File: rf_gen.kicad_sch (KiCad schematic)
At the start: 41 parts, among them J1 Conn_01x07_Male, J2 Conn_01x02_Female, J3 Conn_01x04_Male, J4 Jack-DC, Q1 GS61004B, Q2 G3R350MT12J, U1 NPC81074, U2 AP62150

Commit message: Added Mouser BOM
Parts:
- L8: footprint (none) -> Inductor_SMD:L_0805_2012Metric
- R3, R4: footprint (none) -> Resistor_SMD:R_0805_2012Metric
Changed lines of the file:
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@@
     (property "Reference" "L8" (id 0) (at 200.66 115.57 90))
     (property "Value" "3.3u" (id 1) (at 200.66 118.11 90))
-    (property "Footprint" "" (id 2) (at 200.66 121.92 0)
+    (property "Footprint" "Inductor_SMD:L_0805_2012Metric" (id 2) (at 200.66 121.92 0)
       (effects (font (size 1.27 1.27)) hide)
     )
@@
       (effects (font (size 1.27 1.27)) (justify left))
     )
-    (property "Footprint" "" (id 2) (at 194.056 125.984 90)
+    (property "Footprint" "Resistor_SMD:R_0805_2012Metric" (id 2) (at 194.056 125.984 90)
       (effects (font (size 1.27 1.27)) hide)
     )
@@
       (effects (font (size 1.27 1.27)) (justify left))
     )
-    (property "Footprint" "" (id 2) (at 194.056 136.144 90)
+    (property "Footprint" "Resistor_SMD:R_0805_2012Metric" (id 2) (at 194.056 136.144 90)
       (effects (font (size 1.27 1.27)) hide)
     )
@@
     )
     (path "/12596e45-6707-4319-9f3d-fd07bfb54475"
-      (reference "L8") (unit 1) (value "3.3u") (footprint "")
+      (reference "L8") (unit 1) (value "3.3u") (footprint "Inductor_SMD:L_0805_2012Metric")
     )
     (path "/98c6b453-1edb-41b3-980c-820933811e74"
@@
     )
     (path "/7acdfc10-c7b8-4964-a5bd-7fbb6a01d10b"
-      (reference "R3") (unit 1) (value "52.3k") (footprint "")
+      (reference "R3") (unit 1) (value "52.3k") (footprint "Resistor_SMD:R_0805_2012Metric")
     )
     (path "/7db06bf3-c515-4f51-9e87-096535d2035f"
-      (reference "R4") (unit 1) (value "10k") (footprint "")
+      (reference "R4") (unit 1) (value "10k") (footprint "Resistor_SMD:R_0805_2012Metric")
     )
     (path "/05524bb0-81b6-47ef-ac3c-1b815742ae84"

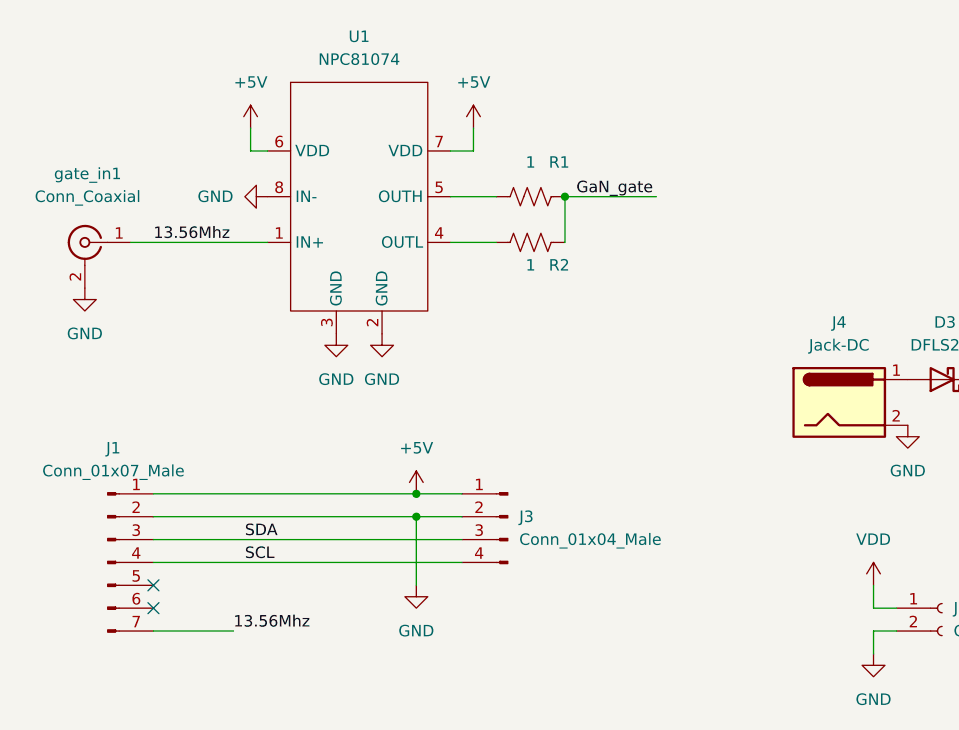
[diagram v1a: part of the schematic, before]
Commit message: Added CoilCraft footprints
Using approximate footprints for the toroids for now
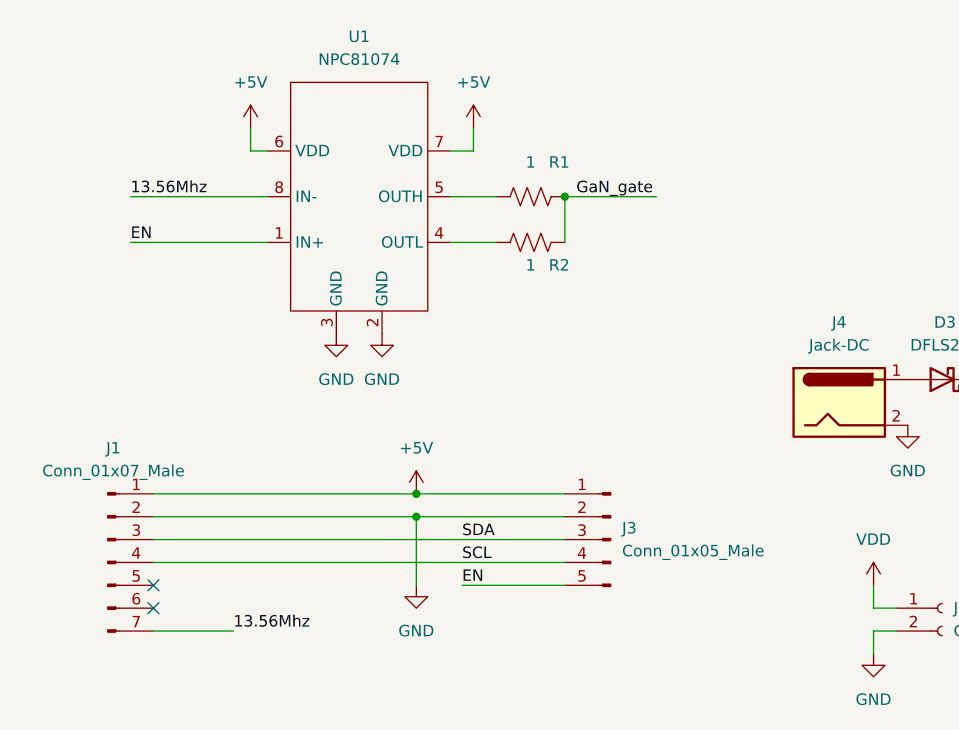
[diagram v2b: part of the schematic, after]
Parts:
- removed J3: Conn_01x04_Male, symbol Connector:Conn_01x04_Male
- removed gate_in1: Conn_Coaxial, Connector_Coaxial:SMA_Amphenol_901-144_Vertical, symbol Connector:Conn_Coaxial
- added J3: Conn_01x05_Male, Connector_PinHeader_2.54mm:PinHeader_1x05_P2.54mm_Vertical, symbol Connector:Conn_01x05_Male
- C13, C15, C16: footprint (none) -> Capacitor_SMD:C_1206_3216Metric
- C14: footprint (none) -> Capacitor_SMD:C_0805_2012Metric
- J1: footprint (none) -> Connector_PinHeader_2.54mm:PinHeader_1x07_P2.54mm_Vertical
- J2: footprint (none) -> Connector_Phoenix_MC_HighVoltage:PhoenixContact_MCV_1,5_2-GF-5.08_1x02_P5.08mm_Vertical_ThreadedFlange
- J4: footprint (none) -> Connector_BarrelJack:BarrelJack_SwitchcraftConxall_RAPC10U_Horizontal
- L1: footprint (none) -> rf_gen:2222SQ-221
- L2, L6: footprint (none) -> Inductor_THT:L_Toroid_Vertical_L10.0mm_W5.0mm_P5.08mm
- L3: footprint (none) -> rf_gen:2222SQ-90N
- L4: footprint (none) -> rf_gen:2222SQ-111
- L5: footprint (none) -> Inductor_THT:L_Axial_L17.5mm_D12.0mm_P20.32mm_Horizontal_Vishay_IM-10-46
- L7: footprint (none) -> Inductor_THT:L_Toroid_Vertical_L28.6mm_W14.3mm_P11.43mm_Bourns_5700
- rf_out1: footprint (none) -> Connector_Coaxial:BNC_TEConnectivity_1478204_Vertical
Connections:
- net +5V: now also J3.1 (Pin_1)
- net 13.56Mhz: now also U1.8 (IN-); no longer U1.1 (IN+)
- net GND: now also J3.2 (Pin_2); no longer U1.8 (IN-)
- net SCL: now also J3.4 (Pin_4)
- net SDA: now also J3.3 (Pin_3)
- new net EN: J3.5 (Pin_5), U1.1 (IN+)

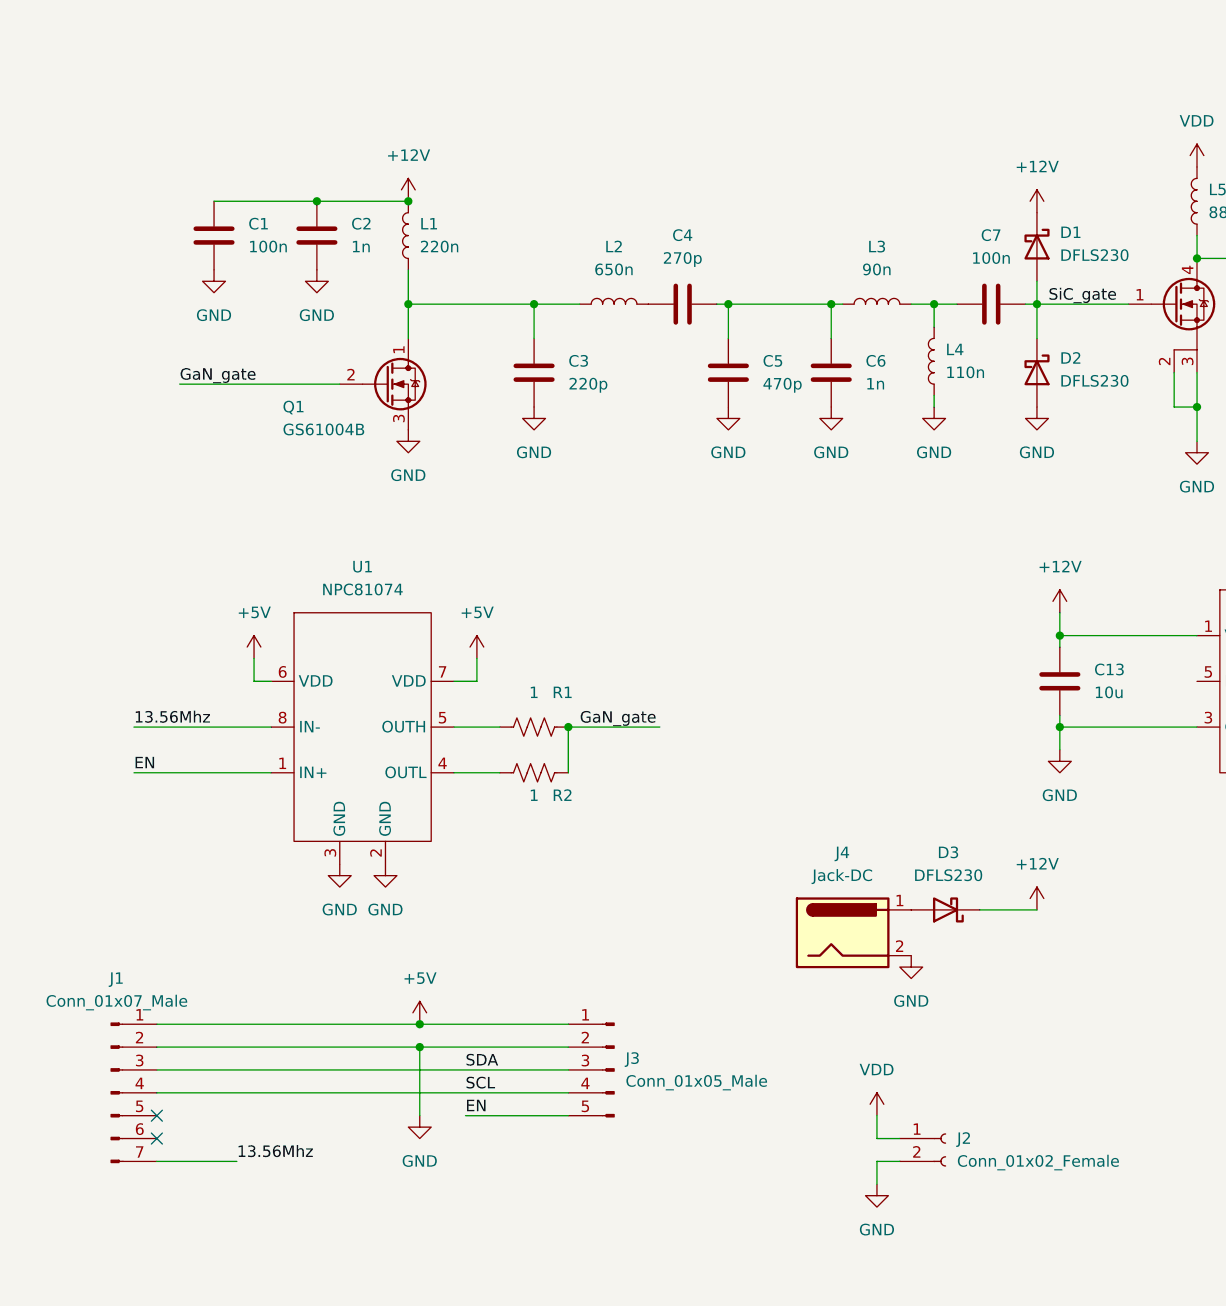
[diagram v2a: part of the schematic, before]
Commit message: First draft of PCB layout
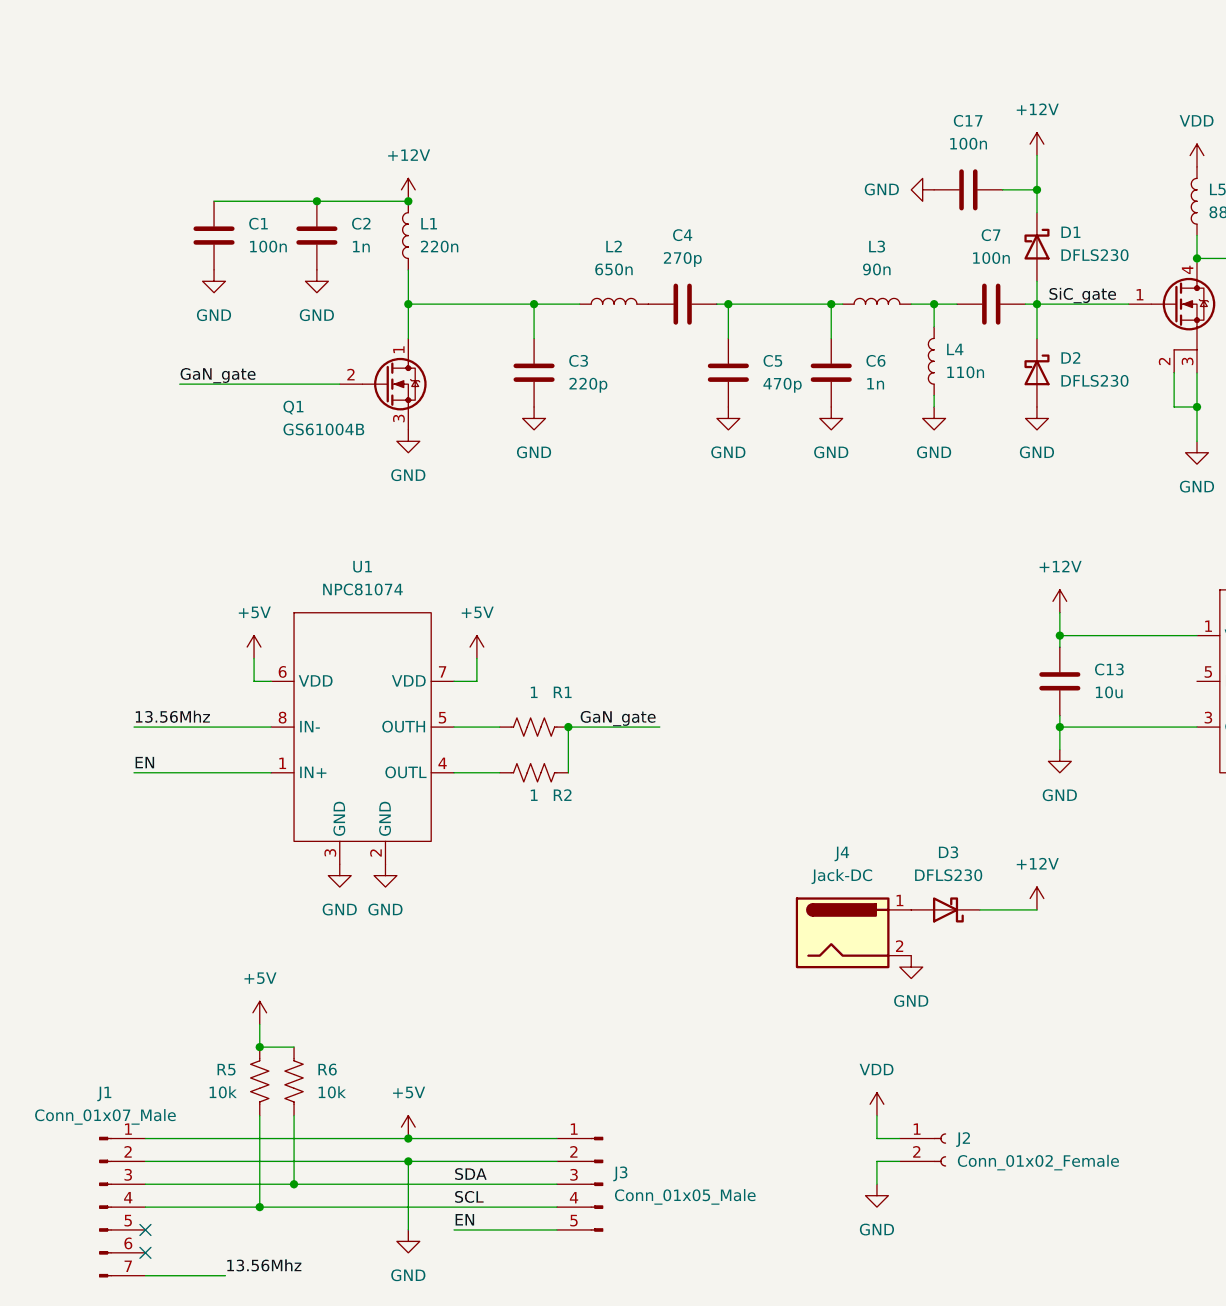
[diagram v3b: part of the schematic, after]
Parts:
- added C17: 100n, Capacitor_SMD:C_1206_3216Metric, symbol Device:C
- added R5, R6: 10k, Resistor_SMD:R_0805_2012Metric, symbol Device:R_US
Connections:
- net +12V: now also C17.2
- net +5V: now also R5.2, R6.1
- net GND: now also C17.1
- net SCL: now also R5.1
- net SDA: now also R6.2
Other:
- moved on the sheet: J1, J3

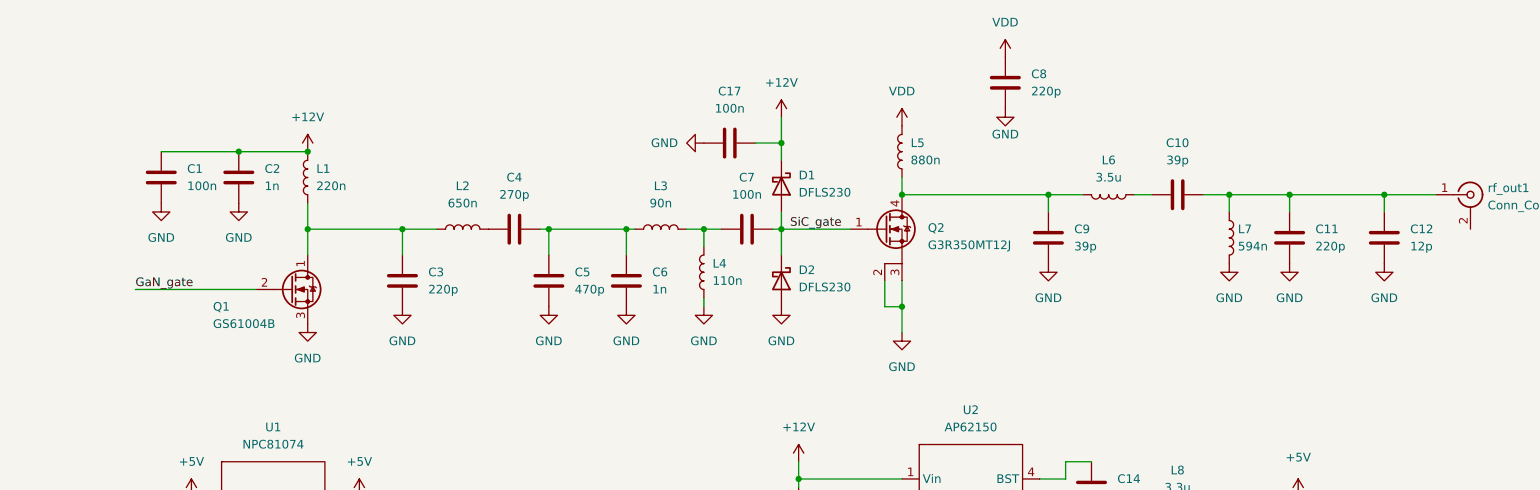
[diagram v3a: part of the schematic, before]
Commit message: Added simulation and design notes
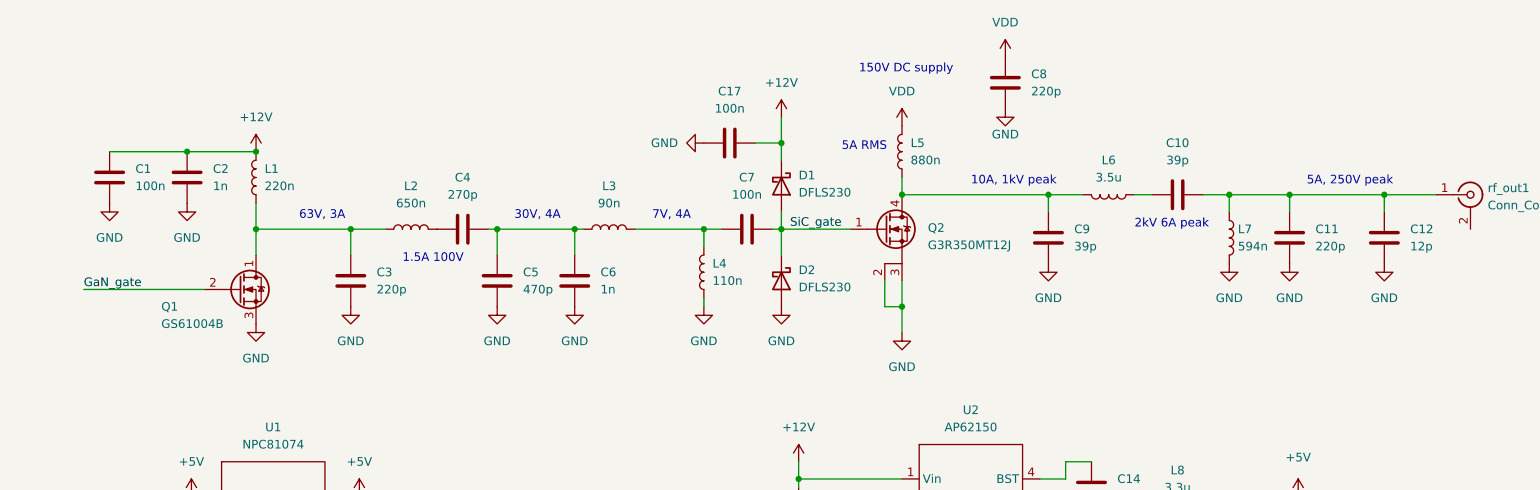
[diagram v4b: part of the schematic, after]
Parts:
- L6: footprint Inductor_THT:L_Toroid_Vertical_L10.0mm_W5.0mm_P5.08mm -> Inductor_THT:L_Toroid_Vertical_L28.6mm_W14.3mm_P11.43mm_Bourns_5700
- L7: footprint Inductor_THT:L_Toroid_Vertical_L28.6mm_W14.3mm_P11.43mm_Bourns_5700 -> Inductor_THT:L_Toroid_Vertical_L10.0mm_W5.0mm_P5.08mm
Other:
- note added: "1.5A 100V"
- note added: "10A, 1kV peak"
- note added: "150V DC supply"
- note added: "2kV 6A peak"
- note added: "30V, 4A"
- note added: "5A RMS"
- note added: "5A, 250V peak"
- note added: "63V, 3A"
- note added: "7V, 4A"
- moved on the sheet: C1, C2, C3, C4, C5, C6, L1, L2, L3, Q1
